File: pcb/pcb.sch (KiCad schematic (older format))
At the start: 14 parts

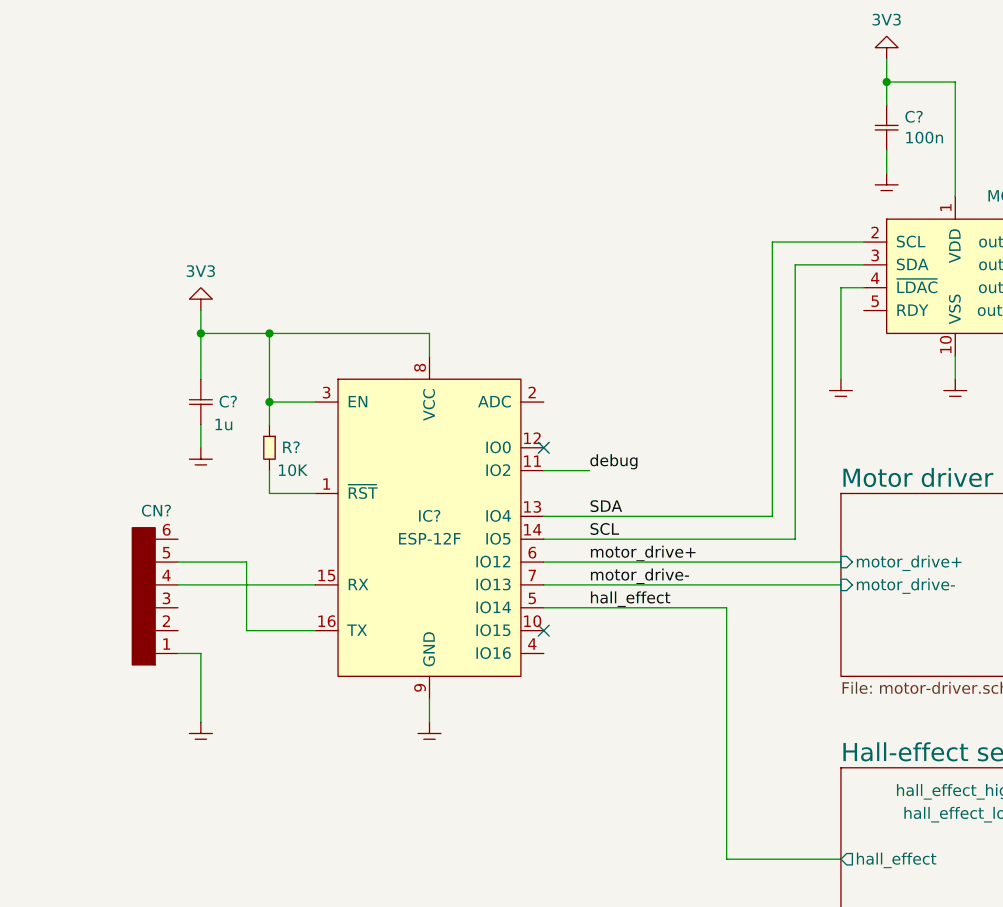
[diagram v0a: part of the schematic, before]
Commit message: added 5V psu and battery voltage to ADC
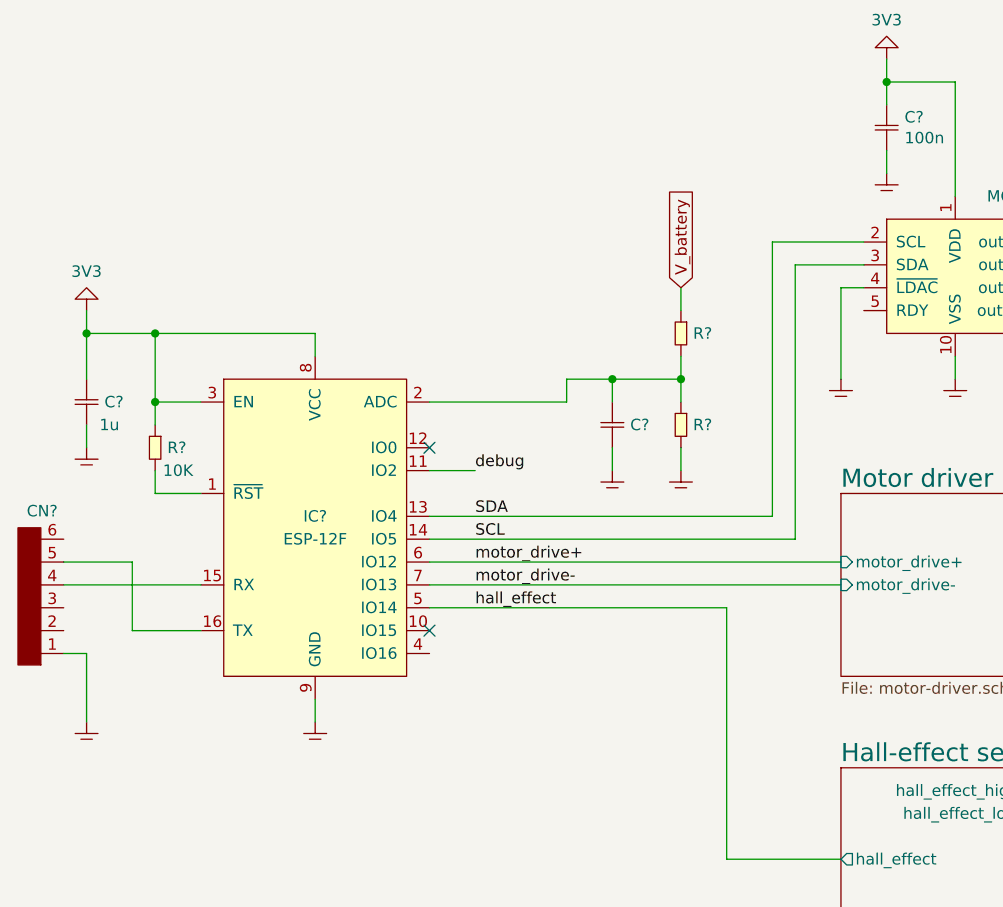
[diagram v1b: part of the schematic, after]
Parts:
- added C?: C, SMT:0603, symbol generic:C
- added GND? (x2): GND, symbol generic:GND
- added R? (x2): R, SMT:0603, symbol generic:R
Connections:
- net GND: now also C?.2, GND?.~ (GND), GND?.~ (GND), R?.2
- net at IC?.2 (ADC): now also C?.1, R?.1, R?.2
- new net V_battery: R?.1
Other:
- moved on the sheet: C?, CN?, IC?, R?

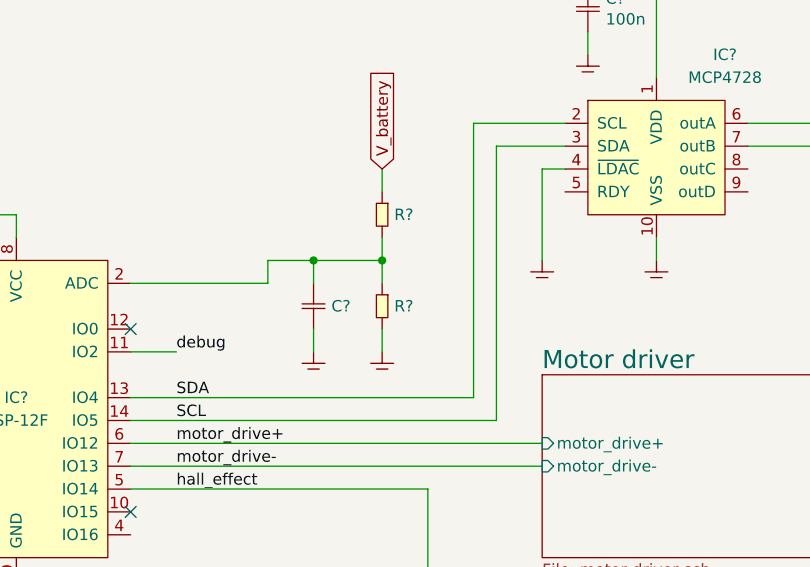
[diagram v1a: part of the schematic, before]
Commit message: added resistor values for battery measurement
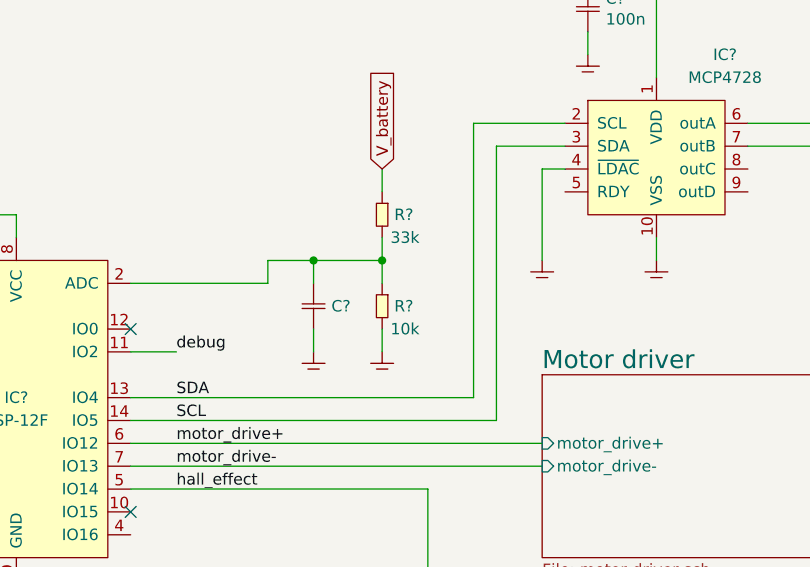
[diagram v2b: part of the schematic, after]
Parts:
- R?: value R -> 33k
- R?: value R -> 10k
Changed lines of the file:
@@
 P 6300 2700
 F 0 "R?" V 6300 2753 50  0000 L CNN
-F 1 "R" H 6300 2600 50  0001 C CNN
+F 1 "33k" V 6400 2800 50  0000 C CNN
 F 2 "SMT:0603" H 6200 2675 50  0001 C CNN
 F 3 "" H 6300 2700 50  0001 C CNN
@@
 P 6300 3100
 F 0 "R?" V 6300 3153 50  0000 L CNN
-F 1 "R" H 6300 3000 50  0001 C CNN
+F 1 "10k" V 6400 3200 50  0000 C CNN
 F 2 "SMT:0603" H 6200 3075 50  0001 C CNN
 F 3 "" H 6300 3100 50  0001 C CNN

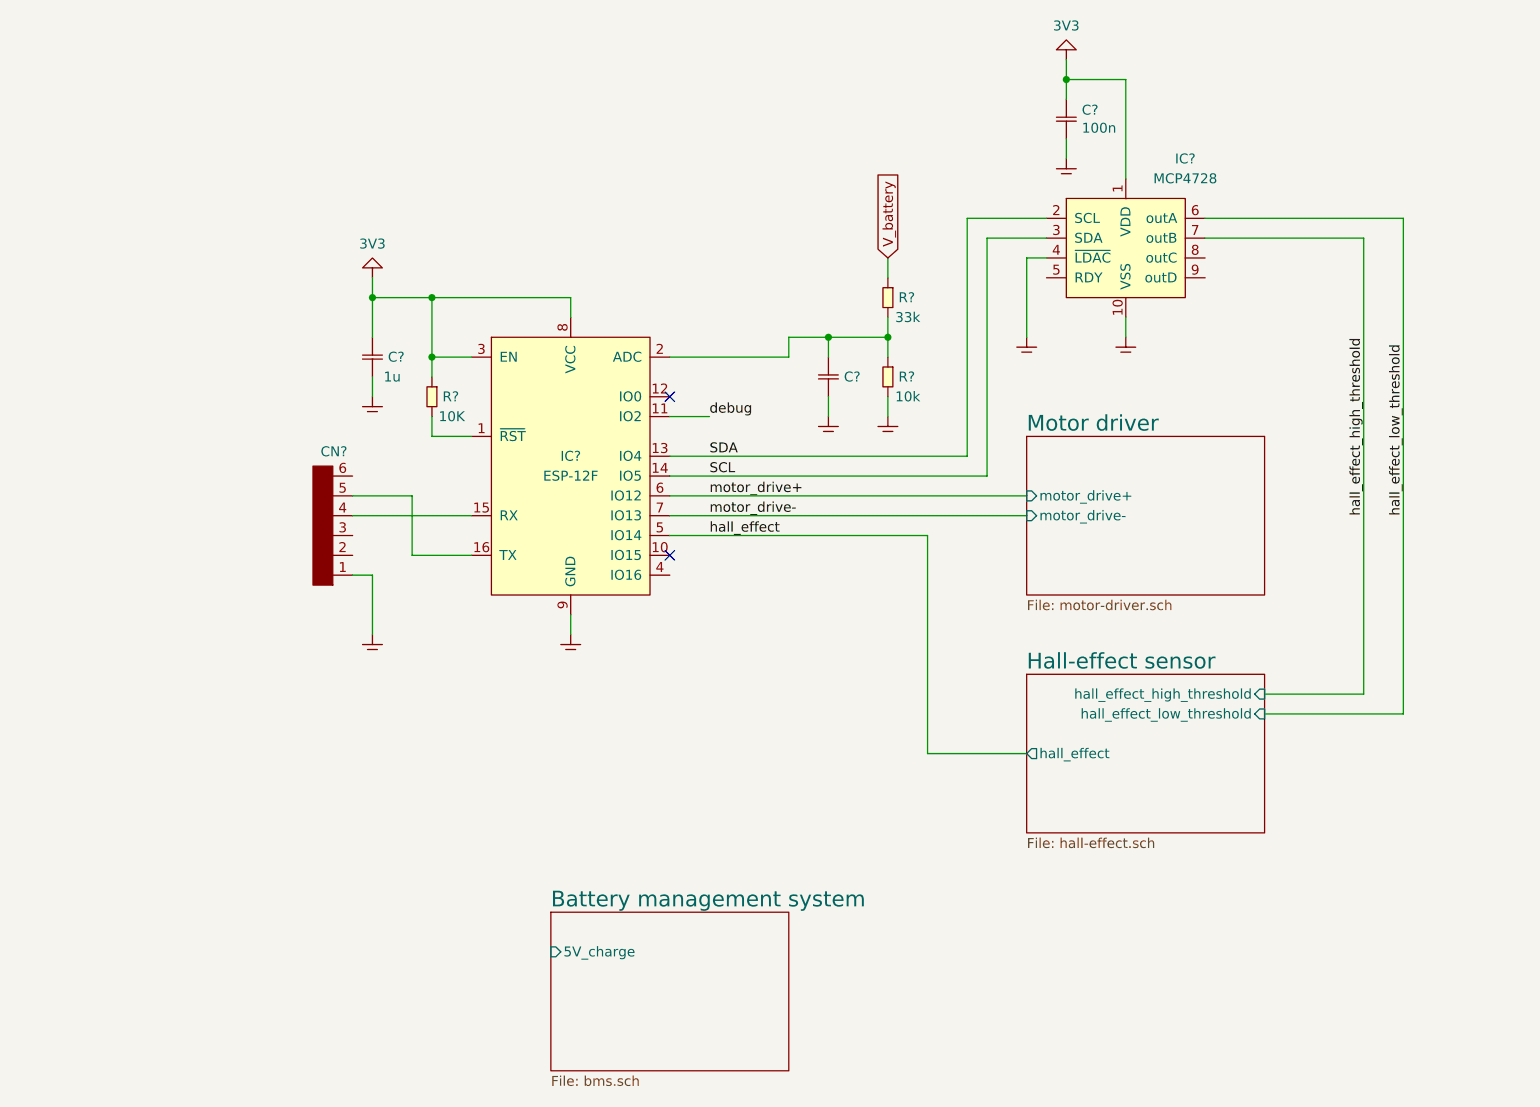
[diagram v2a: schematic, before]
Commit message: added usb interface, switching signal to boost circuits
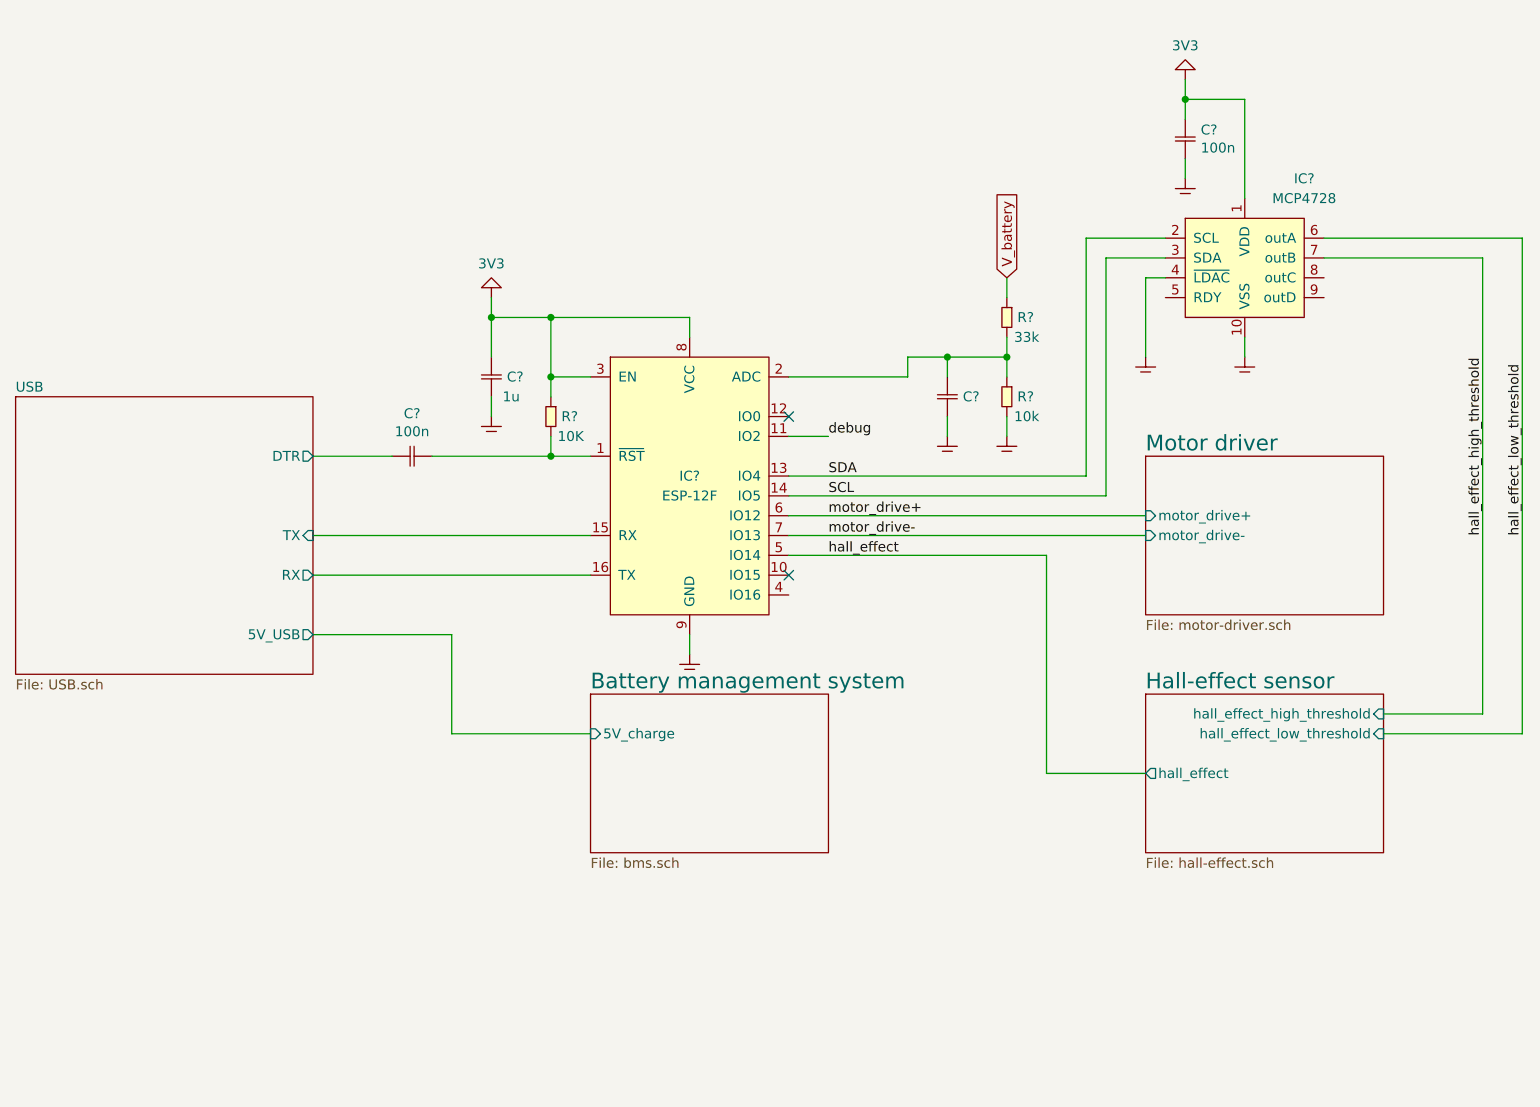
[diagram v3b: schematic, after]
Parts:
- removed CN?: 1x6, pin_headers:1x6, symbol pin_headers:1x6
- removed GND?: GND, symbol generic:GND
- added C?: 100n, SMT:0603, symbol generic:C
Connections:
- net at IC?.1 (~RST), R?.2: now also C?.1
- net USB/TX: now reaches IC?.15 (RX)
- net USB/RX: now reaches IC?.16 (TX)
- new net USB/DTR: C?.2
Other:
- moved on the sheet: C?, IC?, R?

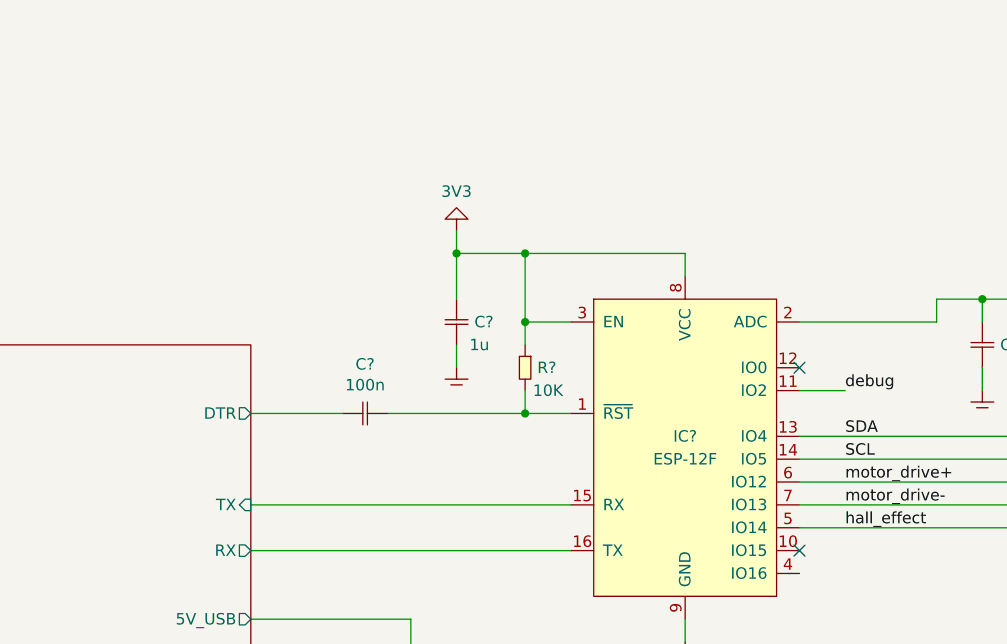
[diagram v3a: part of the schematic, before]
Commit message: added reset switch, DTR to GPIO0
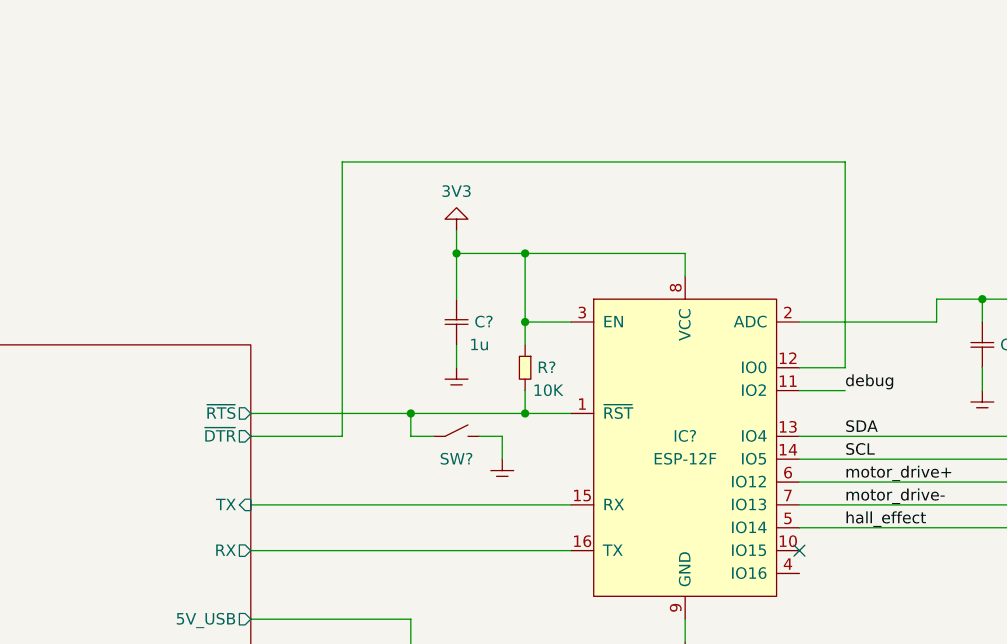
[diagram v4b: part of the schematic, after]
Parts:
- removed C?: 100n, SMT:0603, symbol generic:C
- added GND?: GND, symbol generic:GND
- added SW?: switch_3x4, buttons:sw_3x4, symbol switches:switch_3x4
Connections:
- net GND: now also GND?.~ (GND), SW?.3, SW?.4
- net USB/~RTS: now reaches IC?.1 (~RST), R?.2
- net USB/~RTS: now also SW?.1, SW?.2
- net USB/~DTR: now reaches IC?.12 (IO0)
- no-connect marks 2 -> 1
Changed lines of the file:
@@
 Wire Wire Line
 	5800 3400 6000 3400
-NoConn ~ 5800 3300
 NoConn ~ 5800 4100
 Wire Wire Line
@@
 F3 "TX" I R 3400 3900 50
 F4 "5V_USB" O R 3400 4400 50
-F5 "DTR" O R 3400 3500 50
+F5 "~DTR" O R 3400 3600 50
+F6 "~RTS" O R 3400 3500 50
 $EndSheet
 Wire Wire Line
@@
 Wire Wire Line
 	4100 4900 4800 4900
-$Comp
-L generic:C C?
-U 1 1 5EB843DA
-P 3900 3500
-F 0 "C?" V 3685 3500 50  0000 C CNN
-F 1 "100n" V 3776 3500 50  0000 C CNN
-F 2 "SMT:0603" H 3900 3400 50  0001 C CNN
-F 3 "" H 3900 3500 50  0001 C CNN
-	1    3900 3500
-	0    1    1    0
-$EndComp
-Wire Wire Line
-	3400 3500 3800 3500
-Wire Wire Line
-	4000 3500 4600 3500
 Connection ~ 4600 3500
+Wire Wire Line
+	3400 3600 3800 3600
+Wire Wire Line
+	3800 3600 3800 2400
+Wire Wire Line
+	3800 2400 6000 2400
+Wire Wire Line
+	6000 2400 6000 3300
+Wire Wire Line
+	6000 3300 5800 3300
+$Comp
+L switches:switch_3x4 SW?
+U 1 1 5EB95642
+P 4300 3600
+F 0 "SW?" H 4300 3500 50  0000 C CNN
+F 1 "switch_3x4" H 4300 3700 50  0001 C CNN
+F 2 "buttons:sw_3x4" H 4300 3550 50  0001 C CNN
+F 3 "" H 4300 3600 50  0001 C CNN
+	1    4300 3600
+	1    0    0    -1
+$EndComp
+$Comp
+L generic:GND GND?
+U 1 1 5EB995BD
+P 4500 3700
+F 0 "GND?" H 4650 3750 50  0001 C CNN
+F 1 "GND" H 4650 3700 50  0001 C CNN
+F 2 "" H 4500 3700 50  0001 C CNN
+F 3 "" H 4500 3700 50  0001 C CNN
+	1    4500 3700
+	1    0    0    -1
+$EndComp
+Wire Wire Line
+	3400 3500 4100 3500
+Wire Wire Line
+	4500 3700 4500 3600
+Wire Wire Line
+	4500 3600 4400 3600
+Wire Wire Line
+	4200 3600 4100 3600
+Wire Wire Line
+	4100 3600 4100 3500
+Connection ~ 4100 3500
+Wire Wire Line
+	4100 3500 4600 3500
 $EndSCHEMATC

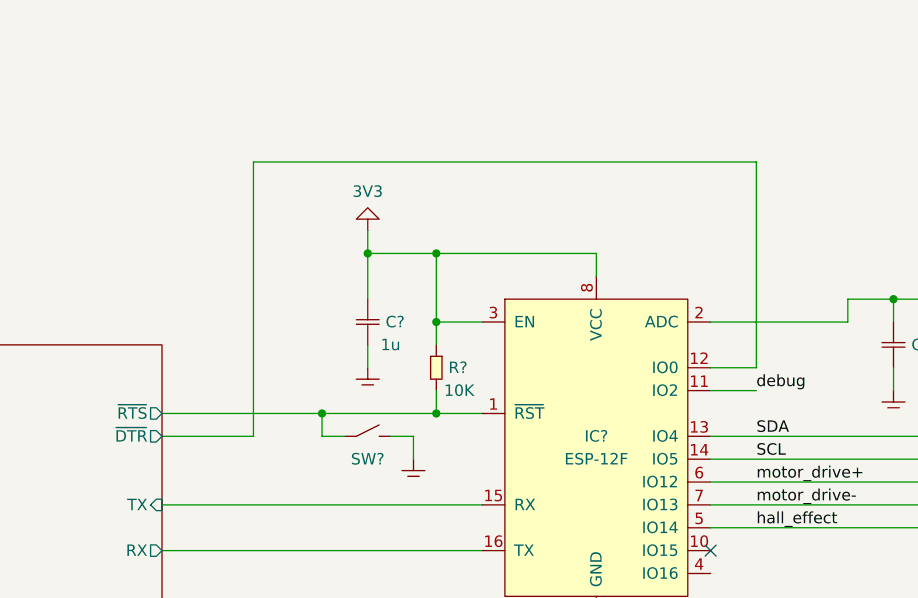
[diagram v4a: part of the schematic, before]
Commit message: added resistor to protect serial adapter
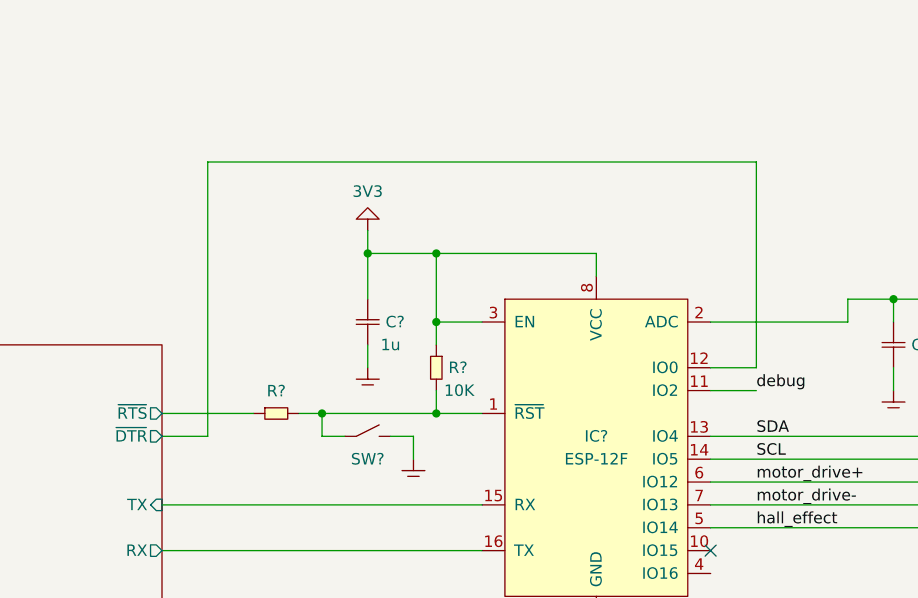
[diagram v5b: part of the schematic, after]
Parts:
- added R?: R, SMT:0603, symbol generic:R
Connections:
- net USB/~RTS: now also R?.1; no longer IC?.1 (~RST), R?.2, SW?.1, SW?.2
- new net: IC?.1 (~RST), R?.2, R?.2, SW?.1, SW?.2
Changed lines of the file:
@@
 Connection ~ 4600 3500
 Wire Wire Line
-	3400 3600 3800 3600
+	3400 3600 3600 3600
 Wire Wire Line
-	3800 3600 3800 2400
+	3600 3600 3600 2400
 Wire Wire Line
-	3800 2400 6000 2400
+	3600 2400 6000 2400
 Wire Wire Line
 	6000 2400 6000 3300
@@
 $EndComp
 Wire Wire Line
-	3400 3500 4100 3500
-Wire Wire Line
 	4500 3700 4500 3600
 Wire Wire Line
@@
 Wire Wire Line
 	4100 3600 4100 3500
-Connection ~ 4100 3500
 Wire Wire Line
 	4100 3500 4600 3500
+$Comp
+L generic:R R?
+U 1 1 5EBA3466
+P 3900 3500
+F 0 "R?" H 3900 3598 50  0000 C CNN
+F 1 "R" H 3900 3400 50  0001 C CNN
+F 2 "SMT:0603" H 3800 3475 50  0001 C CNN
+F 3 "" H 3900 3500 50  0001 C CNN
+	1    3900 3500
+	1    0    0    -1
+$EndComp
+Wire Wire Line
+	3400 3500 3800 3500
+Wire Wire Line
+	4000 3500 4100 3500
+Connection ~ 4100 3500
 $EndSCHEMATC
